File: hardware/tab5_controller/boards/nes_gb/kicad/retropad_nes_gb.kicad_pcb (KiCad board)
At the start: 2 copper layers, 125 x 55 mm, 25 parts, among them J1 Tab5 Ext.Port1, J2 UPDI, SW1 UP, SW2 DOWN, SW3 LEFT, SW4 RIGHT, SW5 B, SW6 A, SW7 SELECT, SW8 START, SW9 MENU, U1 AVR32DD28-I/SO

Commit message: tab5_controller: 0805 hand-solder passives on every board
Swap the 0603 resistors and capacitors (decoupling, I2C pull-ups, reset
pull-up, console-ID straps) for KiCad's 0805 HandSolder footprints, which
have longer pads for soldering by hand. C2 turns 90 degrees so its larger
courtyard clears U1. All four boards are re-routed with Freerouting 1.9;
schematics, BOMs, DRC reports and renders are regenerated.

DRC: 0 errors and 0 unconnected pads on every board (silkscreen and
library-path warnings only). Schematic vs PCB: 0 differences.

Co-Authored-By: Claude Opus 5.5 <noreply@anthropic.com>
Claude-Session: https://claude.ai/code/session_016pgTnJvu7Wh4anaUwDfFmN
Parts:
- C1, C2, C3, C4: footprint Capacitor_SMD:C_0603_1608Metric -> Capacitor_SMD:C_0805_2012Metric_Pad1.18x1.45mm_HandSolder
- R1, R2, R3, R6, R7, R8, R9: footprint Resistor_SMD:R_0603_1608Metric -> Resistor_SMD:R_0805_2012Metric_Pad1.20x1.40mm_HandSolder
- turned C2 to 180 degrees
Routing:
- net +3V3: track 110.0 -> 137.2 mm, vias 1 -> 0
- net SCL: track 44.3 -> 61.5 mm, vias 0 -> 1
- net GND: track 315.8 -> 301.5 mm, vias 1 -> 0
- net ID0: track 32.9 -> 21.3 mm, vias 2 -> 0
- net K_UP: track 53.4 -> 42.0 mm
- net ID1: track 31.1 -> 23.0 mm, vias 2 -> 0
- net SDA: track 43.8 -> 49.9 mm
- net K_B: track 53.8 -> 48.2 mm
- net K_SELECT: track 38.8 -> 35.4 mm
- net ID2: track 19.5 -> 22.4 mm
- net K_START: track 26.1 -> 24.7 mm
- net UPDI: track 31.6 -> 30.7 mm, vias 0 -> 1
- net K_LEFT: track 55.7 -> 55.1 mm
- net K_MENU: track 15.5 -> 15.8 mm, vias 1 -> 0

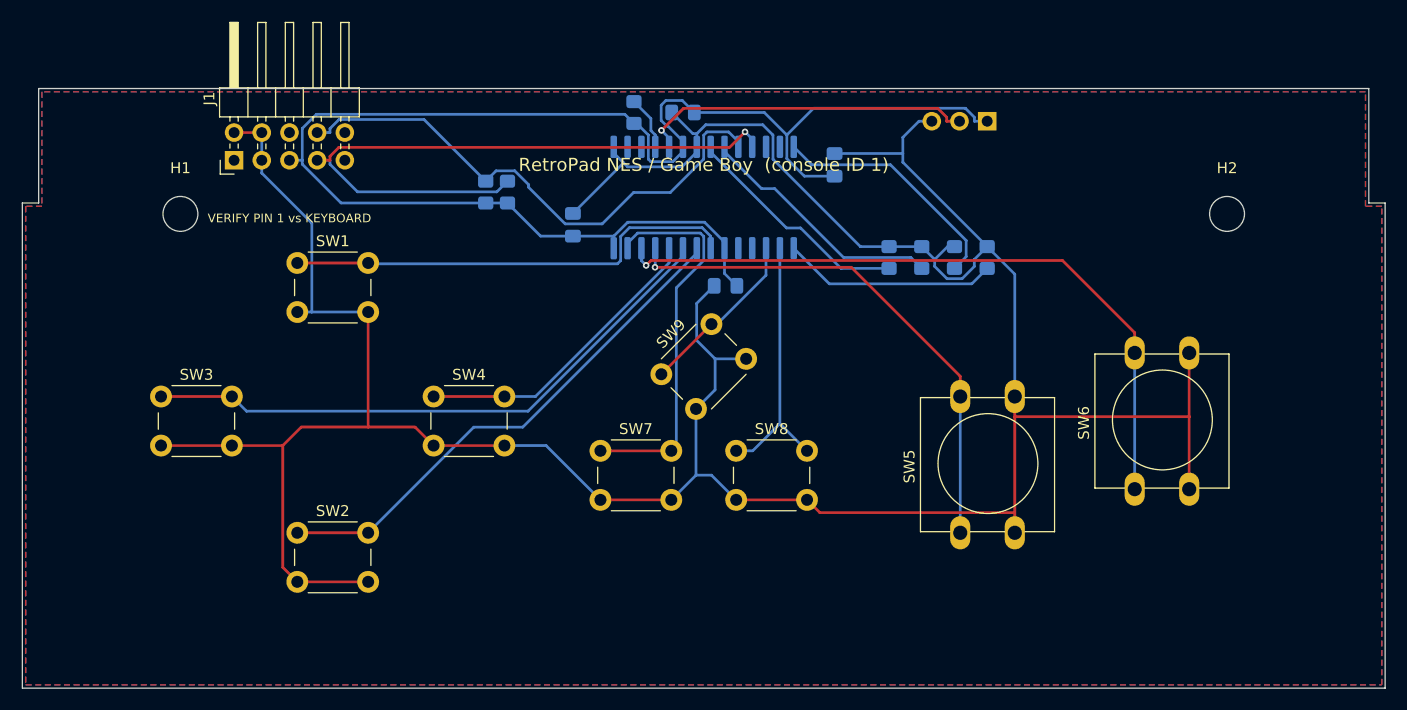
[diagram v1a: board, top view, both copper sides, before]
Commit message: tab5_controller: 4-pin tact switch symbols and footprints
The 6x6 and 12x12 switches are 4-leg parts, and the production layout in
EasyEDA uses their 4-pin symbols, so the KiCad boards now match:

- kicad_lib/RetroPad.pretty: SW_PUSH_6mm_4pin and SW_PUSH-12mm_4pin,
  KiCad's footprints with the pads renumbered 1-4 (pad 1 top-left, then
  clockwise; tied pairs 1-2 and 3-4, the legs 6.5 / 12.5 mm apart).
  gen_pcb.py writes them from the stock footprints and points each
  board's fp-lib-table at the library.
- RetroPad:SW_Push_4pin symbol in gen_sch.py: 1-2 tied, 4-3 tied, one
  contact between. KiCad's 4-pin SW_Push_Dual is a two-contact switch,
  so it doesn't fit these parts.
- Wiring: legs 1-2 to GND, 3-4 to K_<button>. L/R (right angle, two
  contacts plus mounting legs) keep the 2-pin SW_Push.
- All four boards re-routed: DRC 0 unconnected (silkscreen warnings
  only), schematic vs PCB 0 differences, every switch on the pin
  pinmap.h expects; firmware host test passes; Gerber/drill export OK.

Co-Authored-By: Claude Opus 5.5 <noreply@anthropic.com>
Claude-Session: https://claude.ai/code/session_01NhSHTsezreiVZCnuBhQzP2
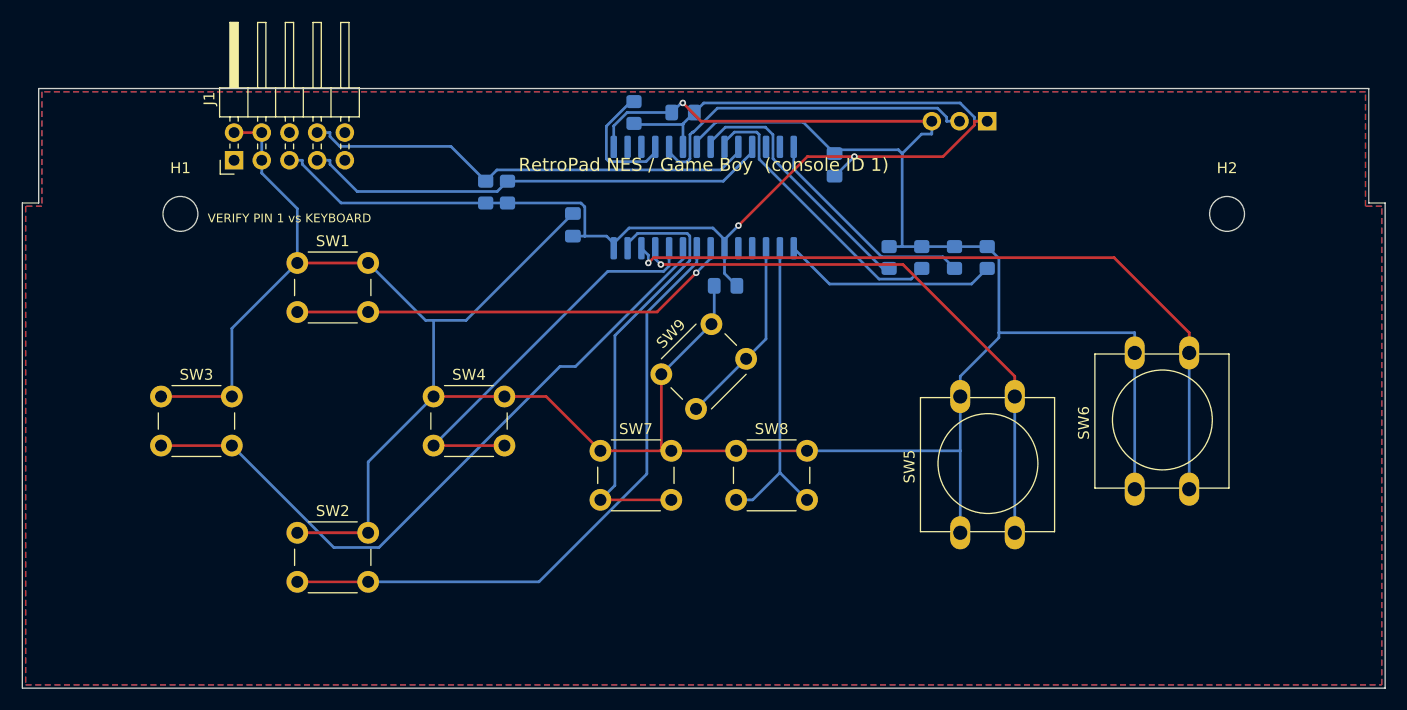
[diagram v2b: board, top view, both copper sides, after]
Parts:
- SW1, SW2, SW3, SW4, SW7, SW8, SW9: footprint Button_Switch_THT:SW_PUSH_6mm -> RetroPad:SW_PUSH_6mm_4pin
- SW5, SW6: footprint Button_Switch_THT:SW_PUSH-12mm -> RetroPad:SW_PUSH-12mm_4pin
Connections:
- SW1 pad 1: K_UP -> GND
- SW2 pad 1: K_DOWN -> GND
- SW3 pad 1: K_LEFT -> GND
- SW4 pad 1: K_RIGHT -> GND
- SW5 pad 1: K_B -> GND
- SW6 pad 1: K_A -> GND
- SW7 pad 1: K_SELECT -> GND
- SW8 pad 1: K_START -> GND
- SW9 pad 1: K_MENU -> GND
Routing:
- net SCL: track 61.5 -> 43.3 mm, vias 1 -> 0
- net +3V3: track 137.2 -> 119.7 mm, vias 0 -> 2
- net K_DOWN: track 47.7 -> 58.8 mm
- net K_LEFT: track 55.1 -> 63.7 mm
- net K_RIGHT: track 28.0 -> 36.6 mm
- net SDA: track 49.9 -> 42.3 mm
- net RESET: track 4.96 -> 11.9 mm
- net GND: track 301.5 -> 295.9 mm, vias 0 -> 1
- net K_SELECT: track 35.4 -> 40.7 mm
- net K_A: track 63.8 -> 68.6 mm
- net K_B: track 48.2 -> 52.8 mm
- net K_START: track 24.7 -> 29.2 mm
- net ID1: track 23.0 -> 26.2 mm
- net ID0: track 21.3 -> 24.0 mm
- net ID2: track 22.4 -> 20.5 mm
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
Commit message: tab5_controller: label each console-ID strap under its own resistor
The back silkscreen printed one mirrored "ID0 ID1 ID2 ID3" string, which
reads left to right from the back while the straps appear right to left
(R9/ID3 first), so the labels were in the reverse order of the parts.
Each strap now gets its own ID<n> label centred under it. Silkscreen
only: the boards keep their routing (same segments and vias), DRC 0
unconnected, schematic vs PCB 0 differences.

Co-Authored-By: Claude Opus 5.5 <noreply@anthropic.com>
Claude-Session: https://claude.ai/code/session_01NhSHTsezreiVZCnuBhQzP2
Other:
- board text added: "ID0"
- board text added: "ID1"
- board text added: "ID2"
- board text added: "ID3"
- board text removed: "ID0 ID1 ID2 ID3"
